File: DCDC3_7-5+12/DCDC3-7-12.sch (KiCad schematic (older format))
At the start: 7 parts, among them U1 XL6009

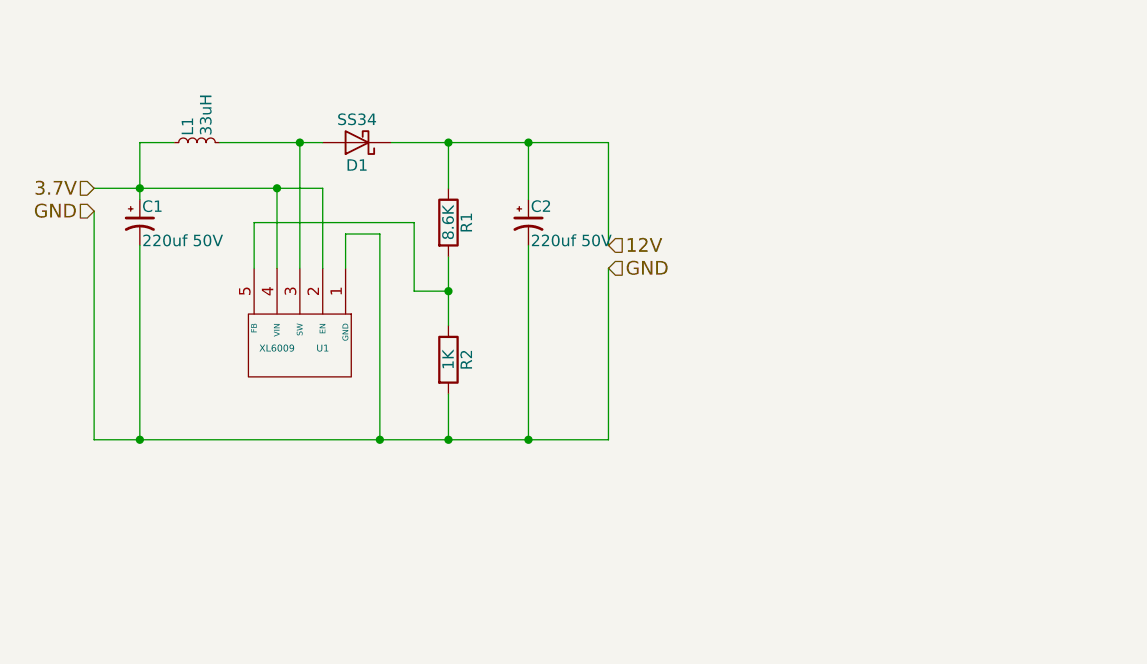
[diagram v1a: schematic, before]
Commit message: Nearly complete circuit for the AUX power supply.
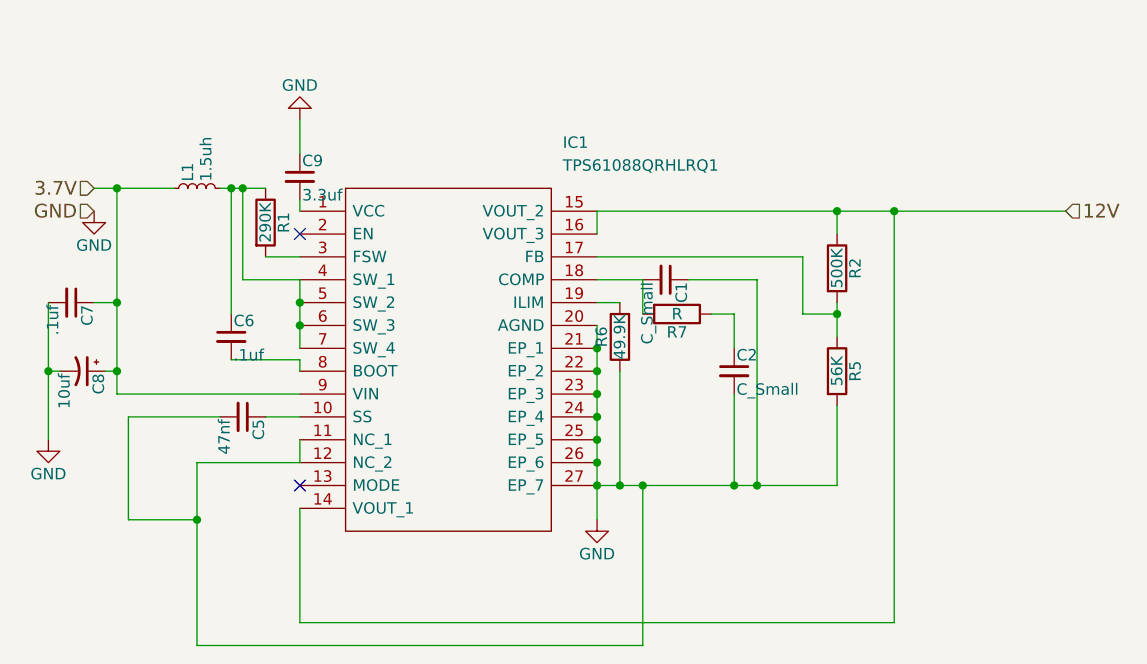
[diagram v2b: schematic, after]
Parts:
- removed C1, C2: 220uf 50V, Capacitors_SMD:CP_Elec_10x10.5, symbol CP1_Small
- removed D1: SS34, Diodes_SMD:D_SMB_Handsoldering, symbol D_Schottky
- removed U1: XL6009, TO_SOT_Packages_SMD:TO-263-5_TabPin3, symbol XL6009
- added C1, C2: C_Small, Capacitors_SMD:C_0402, symbol C_Small
- added C5: 47nf, Capacitors_SMD:C_0402, symbol C_Small
- added C6: .1uf, Capacitors_SMD:C_0201, symbol C_Small
- added C7: .1uf, Capacitors_SMD:C_0402, symbol C_Small
- added C8: 10uf, MyCaps:C_1206_Pol, symbol CP1_Small
- added C9: 3.3uf, Capacitors_SMD:C_0805, symbol C_Small
- added IC1: TPS61088QRHLRQ1, TPS61088QRHLRQ1:TPS61088QRHLRQ1, symbol TPS61088QRHLRQ1
- added R5: 56K, Resistors_SMD:R_0402, symbol R
- added R6: 49.9K, Resistors_SMD:R_0402, symbol R
- added R7: R, Resistors_SMD:R_0402, symbol R
- L1: value 33uH -> 1.5uh; footprint PM5022S-330M-RC:INDPM183140X690N -> Inductors_SMD:L_Wuerth_HCI-7040; Mouser Part Number (none) -> 710-744311150
- R1: value 8.6K -> 290K; footprint Resistors_SMD:R_0805_HandSoldering -> Resistors_SMD:R_0402
- R2: value 1K -> 500K; footprint Resistors_SMD:R_0805_HandSoldering -> Resistors_SMD:R_0402
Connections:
- net 12V: now also R2.1, IC1.14 (VOUT_1), IC1.15 (VOUT_2), IC1.16 (VOUT_3); no longer R1.1
- net 3.7V: now also C7.1, C8.1, IC1.9 (VIN)
- net GND: now also C1.1, C2.2, C5.2, C7.2, C8.2, C9.1, IC1.11 (NC_1), IC1.12 (NC_2), IC1.20 (AGND), IC1.21 (EP_1), IC1.22 (EP_2), IC1.23 (EP_3), IC1.24 (EP_4), IC1.25 (EP_5), IC1.26 (EP_6), IC1.27 (EP_7), R5.2, R6.1; no longer R2.2
- net at L1.2: now also R1.1, C6.1, IC1.4 (SW_1), IC1.5 (SW_2), IC1.6 (SW_3), IC1.7 (SW_4)
- net at R1.2: now also IC1.3 (FSW); no longer R2.1
- new net: C9.2, IC1.1 (VCC)
- new net: C5.1, IC1.10 (SS)
- new net: IC1.17 (FB), R2.2, R5.1
- new net: C1.2, IC1.18 (COMP), R7.2
- new net: IC1.19 (ILIM), R6.2
- new net: C6.2, IC1.8 (BOOT)
- new net: C2.1, R7.1
- no-connect marks 0 -> 2

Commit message: Final version of aux 5v and 12v power supply.
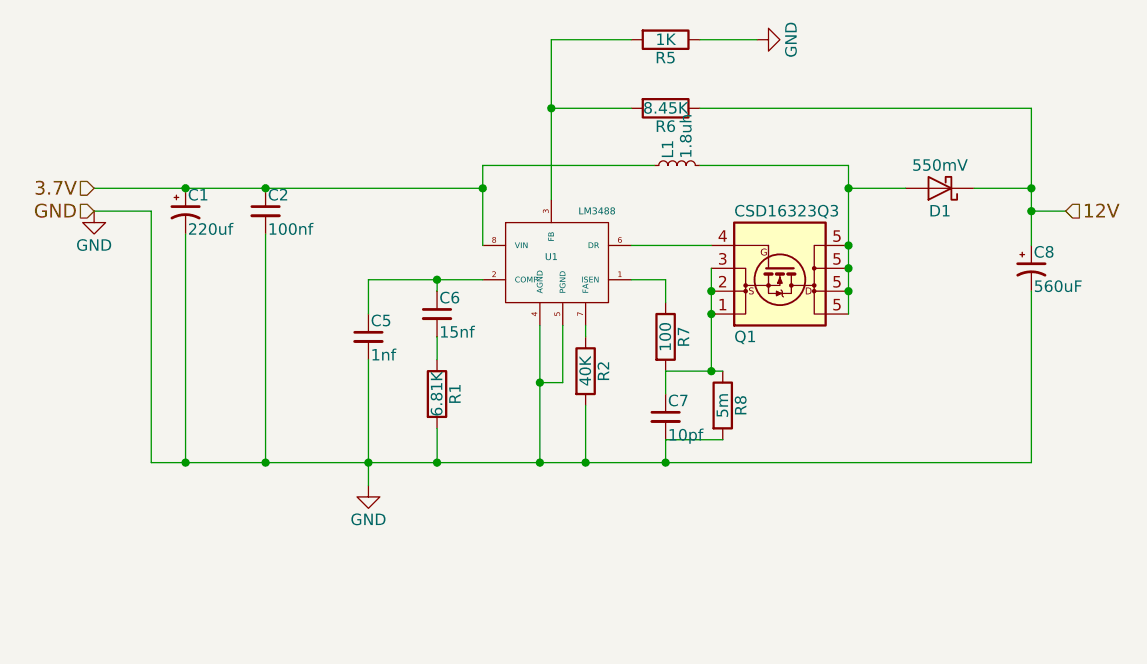
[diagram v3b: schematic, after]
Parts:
- removed C1: C_Small, Capacitors_SMD:C_0402, symbol C_Small
- removed C9: 3.3uf, Capacitors_SMD:C_0805, symbol C_Small
- removed IC1: TPS61088QRHLRQ1, TPS61088QRHLRQ1:TPS61088QRHLRQ1, symbol TPS61088QRHLRQ1
- added C1: 220uf, Capacitors_SMD:CP_Elec_5x5.7, symbol CP1_Small
- added D1: 550mV, Diodes_SMD:D_SMC, symbol D_Schottky
- added Q1: CSD16323Q3, Q3:Q3, symbol CSD16325Q5
- added R8: 5m, Resistors_SMD:R_0612, symbol R
- added U1: LM3488, Housings_SSOP:TSSOP-8_3x3mm_Pitch0.65mm, symbol LM3488
- C2: value C_Small -> 100nf; Mouser Part Number (none) -> 81-GRM155R70J104KA1D
- C5: value 47nf -> 1nf; Mouser Part Number (none) -> 81-GRM1555C1H102JA1J
- C6: value .1uf -> 15nf; footprint Capacitors_SMD:C_0201 -> Capacitors_SMD:C_0805; Mouser Part Number (none) -> 810-CGA4F2C0G1H153J
- C7: value .1uf -> 10pf; footprint Capacitors_SMD:C_0402 -> Capacitors_SMD:C_0805; Mouser Part Number (none) -> 187-CL21C100CBANNNC
- C8: value 10uf -> 560uF; footprint MyCaps:C_1206_Pol -> Capacitors_SMD:CP_Elec_10x10.5; Mouser Part Number (none) -> 667-20SVPF560M
- L1: value 1.5uh -> 1.8uh; footprint Inductors_SMD:L_Wuerth_HCI-7040 -> XAL6030:INDM5564X32N; Mouser Part Number 710-744311150 -> 994-XAL6030-182MEC
- R1: value 290K -> 6.81K; Mouser Part Number (none) -> 71-CRCW0402-6.81K-E3
- R2: value 500K -> 40K; footprint Resistors_SMD:R_0402 -> Resistors_SMD:R_0805; Mouser Part Numbr (none) -> 71-CRCW080540K0FKEA
- R5: value 56K -> 1K; Mouser Part Number (none) -> 71-CRCW0402-1.0K
- R6: value 49.9K -> 8.45K; Mouser Part Number (none) -> 71-CRCW0402-8.45K-E3
- R7: value R -> 100; Mouser Part Number (none) -> 71-CRCW0402100RFKEDC
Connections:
- net 12V: now also C8.1, R6.1, D1.1 (K); no longer R2.1
- net 3.7V: now also C2.1, C1.1, U1.8 (VIN); no longer C7.1, C8.1
- net GND: now also R1.2, R2.2, R5.1, C1.2, R8.2, U1.4 (AGND), U1.5 (PGND); no longer R5.2, R6.1
- net at C5.1: now also C6.1, U1.2 (COMP)
- net at R7.2: now also C7.1, Q1.1 (S), Q1.2 (S), Q1.3 (S), R8.1
- net at R6.2: now also R5.2, U1.3 (FB)
- net at C6.2: now also R1.1
- net at R7.1: now also U1.1 (ISEN); no longer C2.1
- new net: Q1.4 (G), U1.6 (DR)
- new net: R2.1, U1.7 (FA)
- new net: D1.2 (A), L1.2, Q1.5 (D)
- no-connect marks 2 -> 0

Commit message: Final version of aux 5v and 12v power supply.
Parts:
- C1: Mouser Part Number (none) -> 667-6SVPE220MW
- R2: Mouser Part Number (none) -> 71-CRCW080540K0FKEA; Mouser Part Numbr 71-CRCW080540K0FKEA -> (none)
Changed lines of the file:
@@
 12V
 $Comp
-L GND #PWR1
+L GND #PWR01
 U 1 1 62CDA110
 P 4700 3100
-F 0 "#PWR1" H 4700 2850 50  0001 C CNN
+F 0 "#PWR01" H 4700 2850 50  0001 C CNN
 F 1 "GND" H 4700 2950 50  0000 C CNN
 F 2 "" H 4700 3100 50  0001 C CNN
@@
 F 2 "Capacitors_SMD:CP_Elec_5x5.7" H 5100 3100 50  0001 C CNN
 F 3 "" H 5100 3100 50  0001 C CNN
+F 4 "667-6SVPE220MW " H 5100 3100 60  0001 C CNN "Mouser Part Number"
 	1    5100 3100
 	1    0    0    -1
@@
 	6200 4200 6200 4050
 $Comp
-L GND #PWR2
+L GND #PWR02
 U 1 1 62CF4B2E
 P 5900 4300
-F 0 "#PWR2" H 5900 4050 50  0001 C CNN
+F 0 "#PWR02" H 5900 4050 50  0001 C CNN
 F 1 "GND" H 5900 4150 50  0000 C CNN
 F 2 "" H 5900 4300 50  0001 C CNN
@@
 F 2 "Resistors_SMD:R_0805" V 6780 3800 50  0001 C CNN
 F 3 "" H 6850 3800 50  0001 C CNN
-F 4 "71-CRCW080540K0FKEA " V 6850 3800 60  0001 C CNN "Mouser Part Numbr"
+F 4 "71-CRCW080540K0FKEA " V 6850 3800 60  0001 C CNN "Mouser Part Number"
 	1    6850 3800
 	1    0    0    -1
@@
 	6700 2350 7050 2350
 $Comp
-L GND #PWR3
+L GND #PWR03
 U 1 1 62CF5AE6
 P 7600 2350
-F 0 "#PWR3" H 7600 2100 50  0001 C CNN
+F 0 "#PWR03" H 7600 2100 50  0001 C CNN
 F 1 "GND" H 7600 2200 50  0000 C CNN
 F 2 "" H 7600 2350 50  0001 C CNN

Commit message: Final version of aux 5v and 12v power supply.
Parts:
- C8: Mouser Part Number 667-20SVPF560M -> 667-20SVPF560M
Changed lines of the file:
@@
 F 2 "Capacitors_SMD:CP_Elec_10x10.5" H 8800 3350 50  0001 C CNN
 F 3 "" H 8800 3350 50  0001 C CNN
-F 4 " 667-20SVPF560M" H 8800 3350 60  0001 C CNN "Mouser Part Number"
+F 4 "667-20SVPF560M" H 8800 3350 60  0001 C CNN "Mouser Part Number"
 	1    8800 3350
 	1    0    0    -1
